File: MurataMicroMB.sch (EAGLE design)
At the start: 50 parts, among them CON1 C-2395, CON2 WM17143CT-ND, CON3 CON_MIL_10_ARM, CON4 C-2395, IC1 NC7SZ125M5XCT-ND, IC2 296-35164-1-ND, IC3 IC_LPC11U3XQFN33, IC4 AZ1117EH-3.3TRG1DICT-ND, Q1 1253-1168-1-ND, SW1 P-8073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

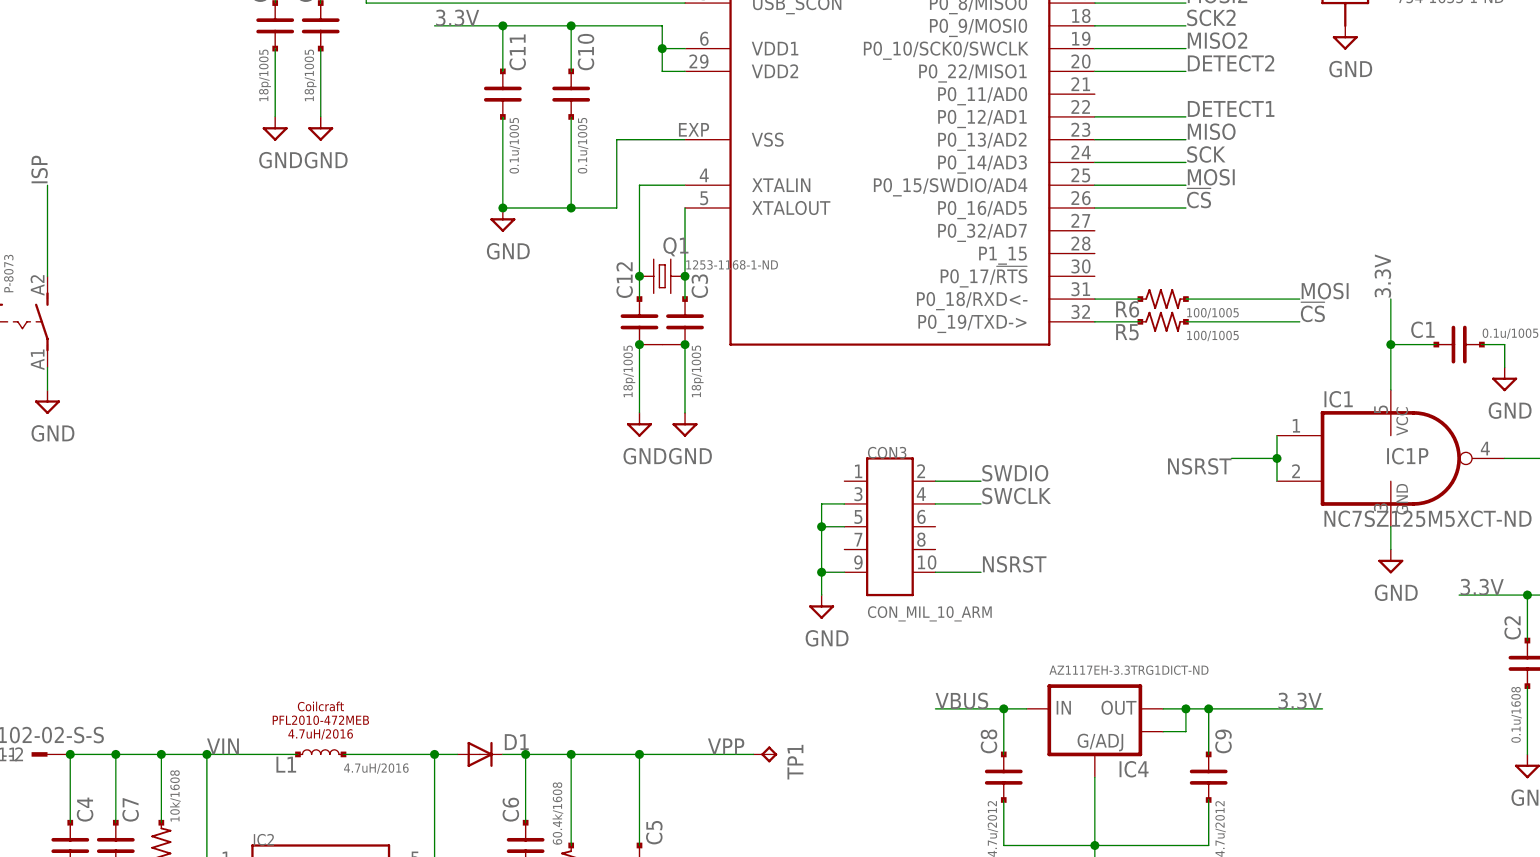
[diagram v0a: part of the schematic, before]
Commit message: [ MB ] add R15/R16 function vs. pin number list
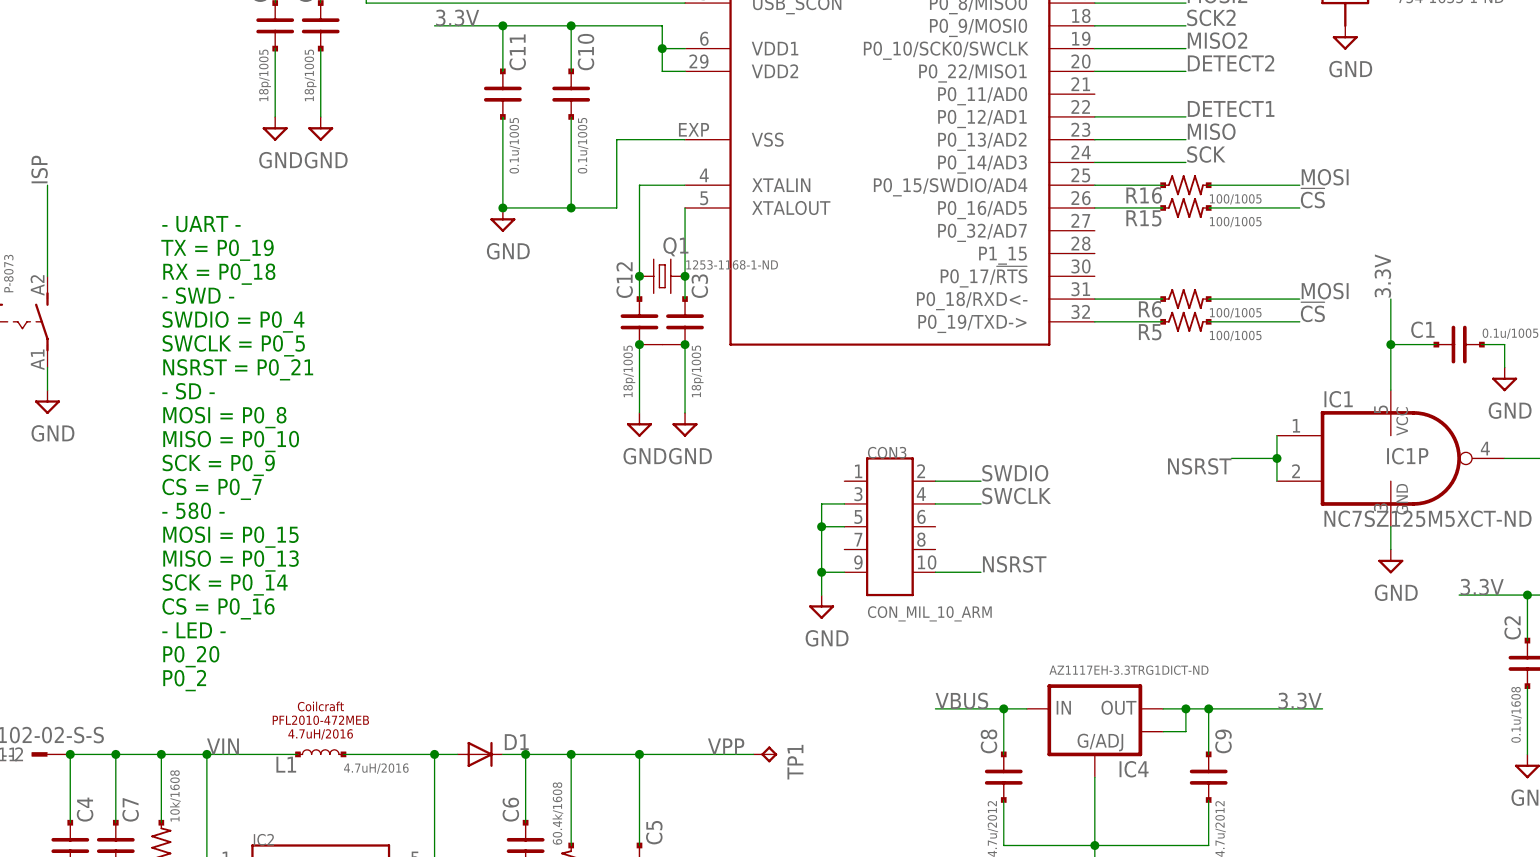
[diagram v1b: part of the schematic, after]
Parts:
- added R15, R16: 100/1005, mylib:R_US_PAD_PAD_1005
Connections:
- new net N$17: IC3.P0_15/SWDIO/AD4, R16.1
- new net N$18: IC3.P0_16/AD5, R15.1
- net !CS!: now also R15.2; no longer IC3.P0_16/AD5
- net MOSI: now also R16.2; no longer IC3.P0_15/SWDIO/AD4
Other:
- note added: "- UART - TX = P0_19 RX = P0_18 - SWD - SWDIO = P0_4 SWCLK = P0_5 NSRST = P0_21 - SD - MOSI = P0_8 MISO = P0_10 SCK = P0_9 CS = P0_7 - 580 - MOSI = P0_15 MISO = P0_13 SCK = P0_14 CS = P0_16 - LED - P0_20 P0_2"
- moved on the sheet: R5, R6
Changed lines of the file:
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@@
 <part name="LED1" library="mylib" deviceset="LED_1SEG_A2K1" device="" value="754-1633-1-ND"/>
 <part name="SUPPLY24" library="mylib" deviceset="GND" device=""/>
+<part name="R15" library="mylib" deviceset="R_US_PAD_PAD" device="_1005" value="100/1005"/>
+<part name="R16" library="mylib" deviceset="R_US_PAD_PAD" device="_1005" value="100/1005"/>
 </parts>
 <sheets>
@@
 <text x="243.84" y="73.66" size="1.27" layer="94" rot="R90" align="center">MurataMicroSD</text>
 <text x="243.84" y="147.32" size="1.27" layer="94" rot="R90" align="center">microSD</text>
+<text x="55.88" y="53.34" size="1.778" layer="91">- UART -
+TX = P0_19
+RX = P0_18
+- SWD -
+SWDIO = P0_4
+SWCLK = P0_5
+NSRST = P0_21
+- SD -
+MOSI = P0_8
+MISO = P0_10
+SCK = P0_9
+CS = P0_7
+- 580 -
+MOSI = P0_15
+MISO = P0_13
+SCK = P0_14
+CS = P0_16
+- LED -
+P0_20
+P0_2</text>
 </plain>
 <instances>
@@
 <instance part="C10" gate="G$1" x="101.6" y="119.38"/>
 <instance part="C11" gate="G$1" x="93.98" y="119.38"/>
-<instance part="R5" gate="G$1" x="167.64" y="93.98"/>
-<instance part="R6" gate="G$1" x="167.64" y="96.52"/>
+<instance part="R5" gate="G$1" x="170.18" y="93.98"/>
+<instance part="R6" gate="G$1" x="170.18" y="96.52"/>
 <instance part="R7" gate="G$1" x="101.6" y="149.86"/>
 <instance part="R8" gate="G$1" x="101.6" y="144.78"/>
@@
 <instance part="LED1" gate="G$1" x="187.96" y="132.08"/>
 <instance part="SUPPLY24" gate="GND" x="187.96" y="124.46"/>
+<instance part="R15" gate="G$1" x="170.18" y="106.68"/>
+<instance part="R16" gate="G$1" x="170.18" y="109.22"/>
 </instances>
 <busses>
@@
 </segment>
 <segment>
-<wire x1="182.88" y1="96.52" x2="170.18" y2="96.52" width="0.1524" layer="91"/>
+<wire x1="182.88" y1="96.52" x2="172.72" y2="96.52" width="0.1524" layer="91"/>
 <pinref part="R6" gate="G$1" pin="2"/>
 <label x="182.88" y="96.52" size="1.778" layer="95"/>
 </segment>
 <segment>
-<wire x1="170.18" y1="109.22" x2="160.02" y2="109.22" width="0.1524" layer="91"/>
-<pinref part="IC3" gate="G$1" pin="P0_15/SWDIO/AD4"/>
-<label x="170.18" y="109.22" size="1.778" layer="95"/>
+<wire x1="182.88" y1="109.22" x2="172.72" y2="109.22" width="0.1524" layer="91"/>
+<label x="182.88" y="109.22" size="1.778" layer="95"/>
+<pinref part="R16" gate="G$1" pin="2"/>
 </segment>
 </net>
@@
 </segment>
 <segment>
-<wire x1="182.88" y1="93.98" x2="170.18" y2="93.98" width="0.1524" layer="91"/>
+<wire x1="182.88" y1="93.98" x2="172.72" y2="93.98" width="0.1524" layer="91"/>
 <pinref part="R5" gate="G$1" pin="2"/>
 <label x="182.88" y="93.98" size="1.778" layer="95"/>
 </segment>
 <segment>
-<wire x1="170.18" y1="106.68" x2="160.02" y2="106.68" width="0.1524" layer="91"/>
-<pinref part="IC3" gate="G$1" pin="P0_16/AD5"/>
-<label x="170.18" y="106.68" size="1.778" layer="95"/>
+<wire x1="182.88" y1="106.68" x2="172.72" y2="106.68" width="0.1524" layer="91"/>
+<label x="182.88" y="106.68" size="1.778" layer="95"/>
+<pinref part="R15" gate="G$1" pin="2"/>
 </segment>
 </net>
@@
 <pinref part="IC3" gate="G$1" pin="P0_18/RXD&lt;-"/>
 <pinref part="R6" gate="G$1" pin="1"/>
-<wire x1="160.02" y1="96.52" x2="165.1" y2="96.52" width="0.1524" layer="91"/>
+<wire x1="160.02" y1="96.52" x2="167.64" y2="96.52" width="0.1524" layer="91"/>
 </segment>
 </net>
@@
 <pinref part="R5" gate="G$1" pin="1"/>
 <pinref part="IC3" gate="G$1" pin="P0_19/TXD-&gt;"/>
-<wire x1="165.1" y1="93.98" x2="160.02" y2="93.98" width="0.1524" layer="91"/>
+<wire x1="167.64" y1="93.98" x2="160.02" y2="93.98" width="0.1524" layer="91"/>
 </segment>
 </net>
@@
 </segment>
 </net>
+<net name="N$17" class="0">
+<segment>
+<pinref part="IC3" gate="G$1" pin="P0_15/SWDIO/AD4"/>
+<pinref part="R16" gate="G$1" pin="1"/>
+<wire x1="167.64" y1="109.22" x2="160.02" y2="109.22" width="0.1524" layer="91"/>
+</segment>
+</net>
+<net name="N$18" class="0">
+<segment>
+<pinref part="IC3" gate="G$1" pin="P0_16/AD5"/>
+<pinref part="R15" gate="G$1" pin="1"/>
+<wire x1="167.64" y1="106.68" x2="160.02" y2="106.68" width="0.1524" layer="91"/>
+</segment>
+</net>

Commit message: [MB] L1 and IC1
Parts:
- IC1: value NC7SZ125M5XCT-ND -> NC7SZ00M5XCT-ND
- L1: value 4.7uH/2016 -> PFL2010-472MEB
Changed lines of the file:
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@@
 <part name="CON1" library="mylib" deviceset="CON_MICROSD" device="_C2395" value="C-2395"/>
 <part name="PCB1" library="dp_pcb" deviceset="PCB_DP_RECTANGLE" device="-43X70" value="PCB_DP_RECTANGLE-43X70"/>
-<part name="IC1" library="74xx-little-us_local" deviceset="74*1G00" device="DBV" technology="LVC" value="NC7SZ125M5XCT-ND"/>
+<part name="IC1" library="74xx-little-us_local" deviceset="74*1G00" device="DBV" technology="LVC" value="NC7SZ00M5XCT-ND"/>
 <part name="CON2" library="mylib" deviceset="CON_USB" device="UB" value="WM17143CT-ND"/>
 <part name="CON3" library="mylib" deviceset="CON_MIL_10" device="_ARM"/>
@@
 <part name="SUPPLY7" library="mylib" deviceset="GND" device=""/>
 <part name="SUPPLY8" library="mylib" deviceset="GND" device=""/>
-<part name="L1" library="mylib" deviceset="INDUCTOR" device="_2016" value="4.7uH/2016"/>
+<part name="L1" library="mylib" deviceset="INDUCTOR" device="_2016" value="PFL2010-472MEB"/>
 <part name="IC2" library="mylib" deviceset="IC_DCDC_LM27313" device="" value="296-35164-1-ND"/>
 <part name="D1" library="mylib" deviceset="DIODE_SMALL" device=""/>
@@
 <instance part="SUPPLY7" gate="GND" x="208.28" y="43.18"/>
 <instance part="SUPPLY8" gate="GND" x="236.22" y="27.94"/>
-<instance part="L1" gate="G$1" x="73.66" y="45.72"/>
+<instance part="L1" gate="G$1" x="73.66" y="45.72" smashed="yes">
+<attribute name="NAME" x="71.12" y="45.466" size="1.778" layer="95" rot="R180"/>
+<attribute name="VALUE" x="71.12" y="43.688" size="1.016" layer="96"/>
+</instance>
 <instance part="IC2" gate="G$1" x="73.66" y="27.94"/>
 <instance part="D1" gate="G$1" x="91.44" y="45.72"/>

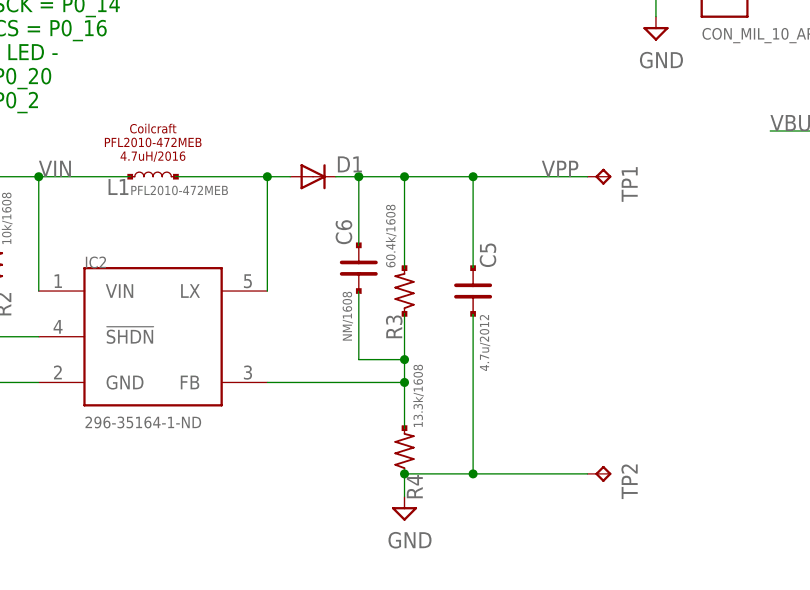
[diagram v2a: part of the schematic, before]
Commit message: [ MB ][ SCH ] R3/4 to use digikey number
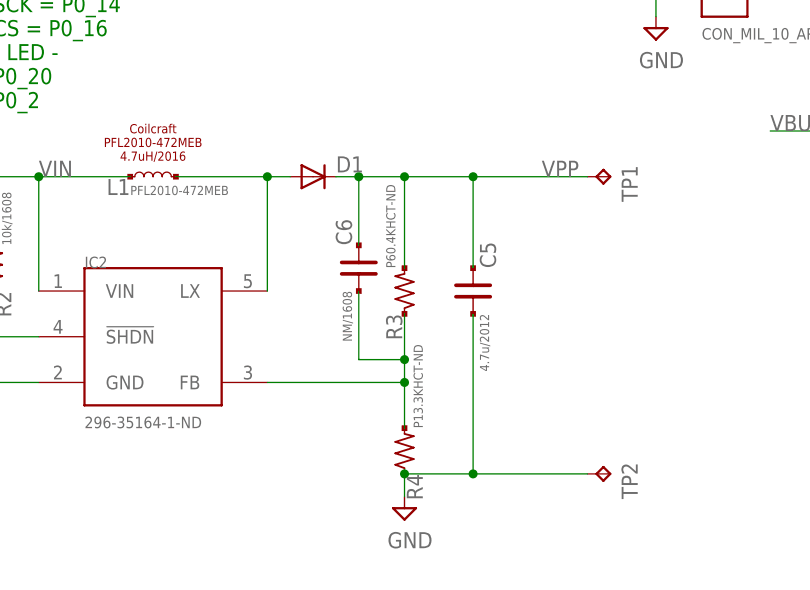
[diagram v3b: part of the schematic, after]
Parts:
- R3: value 60.4k/1608 -> P60.4KHCT-ND
- R4: value 13.3k/1608 -> P13.3KHCT-ND
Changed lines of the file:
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@@
 <part name="D1" library="mylib" deviceset="DIODE_SMALL" device=""/>
 <part name="R2" library="mylib" deviceset="R_US_PAD_PAD" device="_1608" value="10k/1608"/>
-<part name="R3" library="mylib" deviceset="R_US_PAD_PAD" device="_1608" value="60.4k/1608"/>
-<part name="R4" library="mylib" deviceset="R_US_PAD_PAD" device="_1608" value="13.3k/1608"/>
+<part name="R3" library="mylib" deviceset="R_US_PAD_PAD" device="_1608" value="P60.4KHCT-ND"/>
+<part name="R4" library="mylib" deviceset="R_US_PAD_PAD" device="_1608" value="P13.3KHCT-ND"/>
 <part name="C4" library="mylib" deviceset="C_PAD_PAD_" device="2125" value="4.7u/2012"/>
 <part name="C5" library="mylib" deviceset="C_PAD_PAD_" device="2125" value="4.7u/2012"/>

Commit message: [ FIX ] library update
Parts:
- removed TP1, TP2: TPPAD1-13, testpad_local:TPPAD1-13
- added TP3, TP4, TP5: TESTPAD_F, mylib:TESTPAD_F
- added X2: TSW-102-02-S-S, con-samtec.local:TSW-102-02-S-S
- R15, R16, R5, R6: value 100/1005 -> 33/1005
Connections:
- net GND: now also X2-2.1; no longer TP2.TP
- net VPP: now also X2-1.1; no longer TP1.TP
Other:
- note added: "r0.2"
- note removed: "r0.1"
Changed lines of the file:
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@@
 <part name="X1" library="con-samtec.local" deviceset="TSW-102-02-S-S" device=""/>
 <part name="C7" library="mylib" deviceset="C_PAD_PAD_" device="1608" value="0.1u/1608"/>
-<part name="TP1" library="testpad_local" deviceset="TP" device="PAD1-13"/>
-<part name="TP2" library="testpad_local" deviceset="TP" device="PAD1-13"/>
 <part name="IC3" library="mylib" deviceset="IC_LPC11U3XQFN33" device=""/>
 <part name="C8" library="mylib" deviceset="C_PAD_PAD_" device="2125" value="4.7u/2012"/>
@@
 <part name="C10" library="mylib" deviceset="C_PAD_PAD_" device="1005" value="0.1u/1005"/>
 <part name="C11" library="mylib" deviceset="C_PAD_PAD_" device="1005" value="0.1u/1005"/>
-<part name="R5" library="mylib" deviceset="R_US_PAD_PAD" device="_1005" value="100/1005"/>
-<part name="R6" library="mylib" deviceset="R_US_PAD_PAD" device="_1005" value="100/1005"/>
+<part name="R5" library="mylib" deviceset="R_US_PAD_PAD" device="_1005" value="33/1005"/>
+<part name="R6" library="mylib" deviceset="R_US_PAD_PAD" device="_1005" value="33/1005"/>
 <part name="R7" library="mylib" deviceset="R_US_PAD_PAD" device="_1005" value="10k/1005"/>
 <part name="R8" library="mylib" deviceset="R_US_PAD_PAD" device="_1005" value="10k/1005"/>
@@
 <part name="LED1" library="mylib" deviceset="LED_1SEG_A2K1" device="" value="754-1633-1-ND"/>
 <part name="SUPPLY24" library="mylib" deviceset="GND" device=""/>
-<part name="R15" library="mylib" deviceset="R_US_PAD_PAD" device="_1005" value="100/1005"/>
-<part name="R16" library="mylib" deviceset="R_US_PAD_PAD" device="_1005" value="100/1005"/>
+<part name="R15" library="mylib" deviceset="R_US_PAD_PAD" device="_1005" value="33/1005"/>
+<part name="R16" library="mylib" deviceset="R_US_PAD_PAD" device="_1005" value="33/1005"/>
+<part name="TP3" library="mylib" deviceset="TESTPAD" device="_F"/>
+<part name="TP4" library="mylib" deviceset="TESTPAD" device="_F"/>
+<part name="TP5" library="mylib" deviceset="TESTPAD" device="_F"/>
+<part name="X2" library="con-samtec.local" deviceset="TSW-102-02-S-S" device=""/>
 </parts>
 <sheets>
 <sheet>
 <plain>
-<text x="162.56" y="5.08" size="12.7" layer="94">r0.1</text>
+<text x="162.56" y="5.08" size="12.7" layer="94">r0.2</text>
 <text x="73.66" y="49.53" size="1.016" layer="94" align="center">Coilcraft
 PFL2010-472MEB
@@
 <instance part="X1" gate="-2" x="43.18" y="45.72" rot="R180"/>
 <instance part="C7" gate="G$1" x="50.8" y="35.56"/>
-<instance part="TP1" gate="G$1" x="124.46" y="45.72" rot="R270"/>
-<instance part="TP2" gate="G$1" x="124.46" y="12.7" rot="R270"/>
 <instance part="IC3" gate="G$1" x="137.16" y="154.94"/>
 <instance part="C8" gate="G$1" x="149.86" y="43.18" rot="MR0"/>
@@
 <instance part="R15" gate="G$1" x="170.18" y="106.68"/>
 <instance part="R16" gate="G$1" x="170.18" y="109.22"/>
+<instance part="TP3" gate="1" x="149.86" y="7.62"/>
+<instance part="TP4" gate="1" x="149.86" y="10.16"/>
+<instance part="TP5" gate="1" x="149.86" y="12.7"/>
+<instance part="X2" gate="-1" x="124.46" y="45.72"/>
+<instance part="X2" gate="-2" x="124.46" y="12.7"/>
 </instances>
 <busses>
@@
 <pinref part="C5" gate="G$1" pin="2"/>
 <wire x1="109.22" y1="12.7" x2="109.22" y2="30.48" width="0.1524" layer="91"/>
-<pinref part="TP2" gate="G$1" pin="TP"/>
 <wire x1="109.22" y1="12.7" x2="121.92" y2="12.7" width="0.1524" layer="91"/>
 <junction x="109.22" y="12.7"/>
+<pinref part="X2" gate="-2" pin="1"/>
 </segment>
 <segment>
@@
 <junction x="109.22" y="45.72"/>
 <label x="116.84" y="45.72" size="1.778" layer="95"/>
-<pinref part="TP1" gate="G$1" pin="TP"/>
-</segment>
-</net>
+<pinref part="X2" gate="-1" pin="1"/>
+</segment>
+</net>

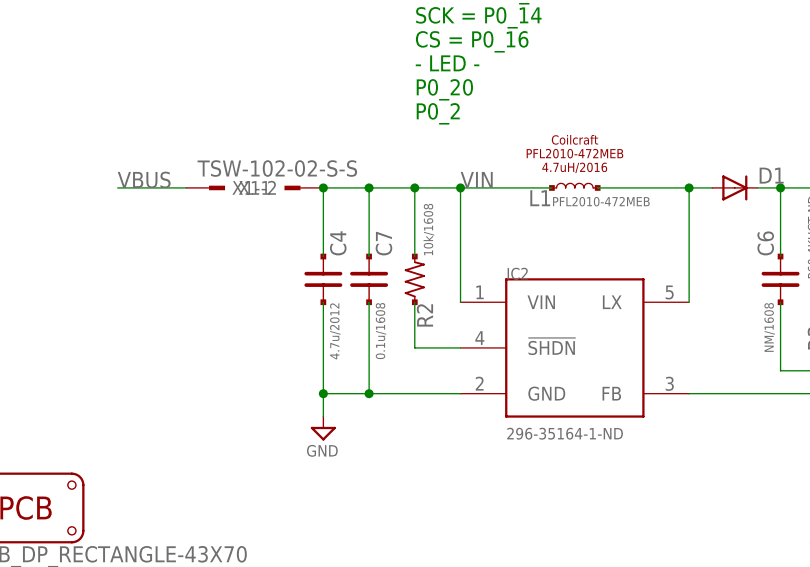
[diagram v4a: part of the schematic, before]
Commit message: [ MB ] resize R2 and C7
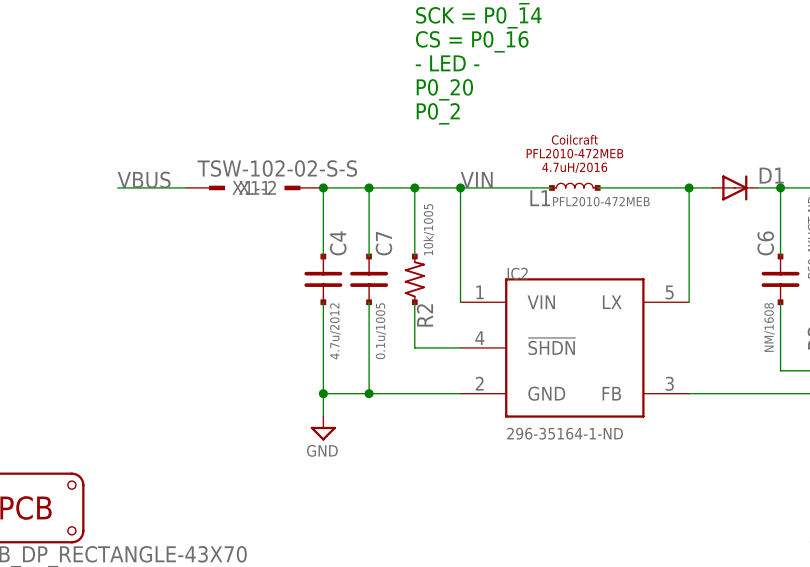
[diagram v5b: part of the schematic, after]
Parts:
- C7: value 0.1u/1608 -> 0.1u/1005; device mylib:C_PAD_PAD_1608 -> mylib:C_PAD_PAD_1005
- R2: value 10k/1608 -> 10k/1005; device mylib:R_US_PAD_PAD_1608 -> mylib:R_US_PAD_PAD_1005
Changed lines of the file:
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@@
 <part name="IC2" library="mylib" deviceset="IC_DCDC_LM27313" device="" value="296-35164-1-ND"/>
 <part name="D1" library="mylib" deviceset="DIODE_SMALL" device=""/>
-<part name="R2" library="mylib" deviceset="R_US_PAD_PAD" device="_1608" value="10k/1608"/>
+<part name="R2" library="mylib" deviceset="R_US_PAD_PAD" device="_1005" value="10k/1005"/>
 <part name="R3" library="mylib" deviceset="R_US_PAD_PAD" device="_1608" value="P60.4KHCT-ND"/>
 <part name="R4" library="mylib" deviceset="R_US_PAD_PAD" device="_1608" value="P13.3KHCT-ND"/>
@@
 <part name="SUPPLY11" library="mylib" deviceset="GND" device=""/>
 <part name="X1" library="con-samtec.local" deviceset="TSW-102-02-S-S" device=""/>
-<part name="C7" library="mylib" deviceset="C_PAD_PAD_" device="1608" value="0.1u/1608"/>
+<part name="C7" library="mylib" deviceset="C_PAD_PAD_" device="1005" value="0.1u/1005"/>
 <part name="IC3" library="mylib" deviceset="IC_LPC11U3XQFN33" device=""/>
 <part name="C8" library="mylib" deviceset="C_PAD_PAD_" device="2125" value="4.7u/2012"/>
